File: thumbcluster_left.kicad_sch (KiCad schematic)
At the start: 12 parts, among them J1 Conn_01x06_Female, J2 Conn_01x06_Female, SW1 SW_Push, SW2 SW_Push, SW3 SW_Push, SW4 SW_Push, SW5 SW_Push

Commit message: Through hole switches
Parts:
- SW1, SW2, SW3, SW4, SW5: footprint keyswitches:Kailh_socket_MX -> keyswitches:SW_MX
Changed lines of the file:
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@@
     (property "Reference" "SW2" (id 0) (at 90.17 55.245 0))
     (property "Value" "SW_Push" (id 1) (at 90.17 57.785 0))
-    (property "Footprint" "keyswitches:Kailh_socket_MX" (id 2) (at 90.17 58.42 0)
+    (property "Footprint" "keyswitches:SW_MX" (id 2) (at 90.17 58.42 0)
       (effects (font (size 1.27 1.27)) hide)
     )
@@
     (property "Reference" "SW3" (id 0) (at 113.03 55.245 0))
     (property "Value" "SW_Push" (id 1) (at 113.03 57.785 0))
-    (property "Footprint" "keyswitches:Kailh_socket_MX" (id 2) (at 113.03 58.42 0)
+    (property "Footprint" "keyswitches:SW_MX" (id 2) (at 113.03 58.42 0)
       (effects (font (size 1.27 1.27)) hide)
     )
@@
     (property "Reference" "SW4" (id 0) (at 136.525 55.245 0))
     (property "Value" "SW_Push" (id 1) (at 136.525 57.785 0))
-    (property "Footprint" "keyswitches:Kailh_socket_MX" (id 2) (at 136.525 58.42 0)
+    (property "Footprint" "keyswitches:SW_MX" (id 2) (at 136.525 58.42 0)
       (effects (font (size 1.27 1.27)) hide)
     )
@@
     (property "Reference" "SW1" (id 0) (at 62.865 55.245 0))
     (property "Value" "SW_Push" (id 1) (at 62.865 57.785 0))
-    (property "Footprint" "keyswitches:Kailh_socket_MX" (id 2) (at 62.865 58.42 0)
+    (property "Footprint" "keyswitches:SW_MX" (id 2) (at 62.865 58.42 0)
       (effects (font (size 1.27 1.27)) hide)
     )
@@
     (property "Reference" "SW5" (id 0) (at 161.925 54.61 0))
     (property "Value" "SW_Push" (id 1) (at 161.925 57.15 0))
-    (property "Footprint" "keyswitches:Kailh_socket_MX" (id 2) (at 161.925 57.785 0)
+    (property "Footprint" "keyswitches:SW_MX" (id 2) (at 161.925 57.785 0)
       (effects (font (size 1.27 1.27)) hide)
     )
@@
     )
     (path "/85b19fe2-44d2-475f-bbc1-af68021ea01a"
-      (reference "SW1") (unit 1) (value "SW_Push") (footprint "keyswitches:Kailh_socket_MX")
+      (reference "SW1") (unit 1) (value "SW_Push") (footprint "keyswitches:SW_MX")
     )
     (path "/0c81e866-4681-43a4-aa9d-b943506b0b37"
-      (reference "SW2") (unit 1) (value "SW_Push") (footprint "keyswitches:Kailh_socket_MX")
+      (reference "SW2") (unit 1) (value "SW_Push") (footprint "keyswitches:SW_MX")
     )
     (path "/18a7139e-6ff8-49c2-a6d5-d2f8a6857830"
-      (reference "SW3") (unit 1) (value "SW_Push") (footprint "keyswitches:Kailh_socket_MX")
+      (reference "SW3") (unit 1) (value "SW_Push") (footprint "keyswitches:SW_MX")
     )
     (path "/8185e278-47e0-4401-93fe-75e7b14ab53c"
-      (reference "SW4") (unit 1) (value "SW_Push") (footprint "keyswitches:Kailh_socket_MX")
+      (reference "SW4") (unit 1) (value "SW_Push") (footprint "keyswitches:SW_MX")
     )
     (path "/ecba316e-704e-4ac5-90f8-4ebc6db6ba65"
-      (reference "SW5") (unit 1) (value "SW_Push") (footprint "keyswitches:Kailh_socket_MX")
-    )
-  )
+      (reference "SW5") (unit 1) (value "SW_Push") (footprint "keyswitches:SW_MX")
+    )
+  )

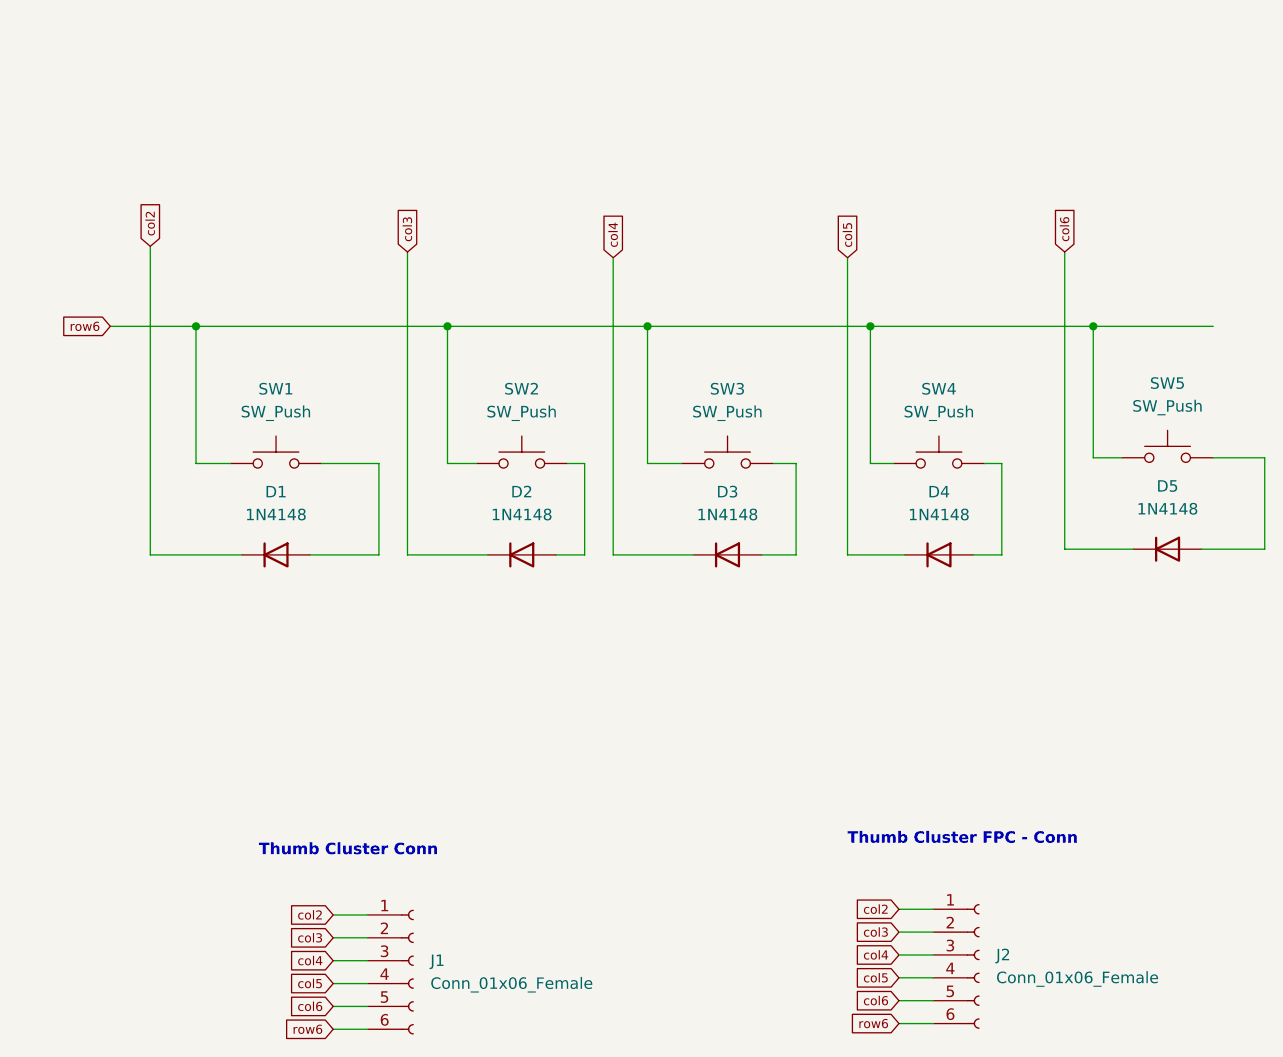
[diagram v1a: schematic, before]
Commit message: Complete net refactor
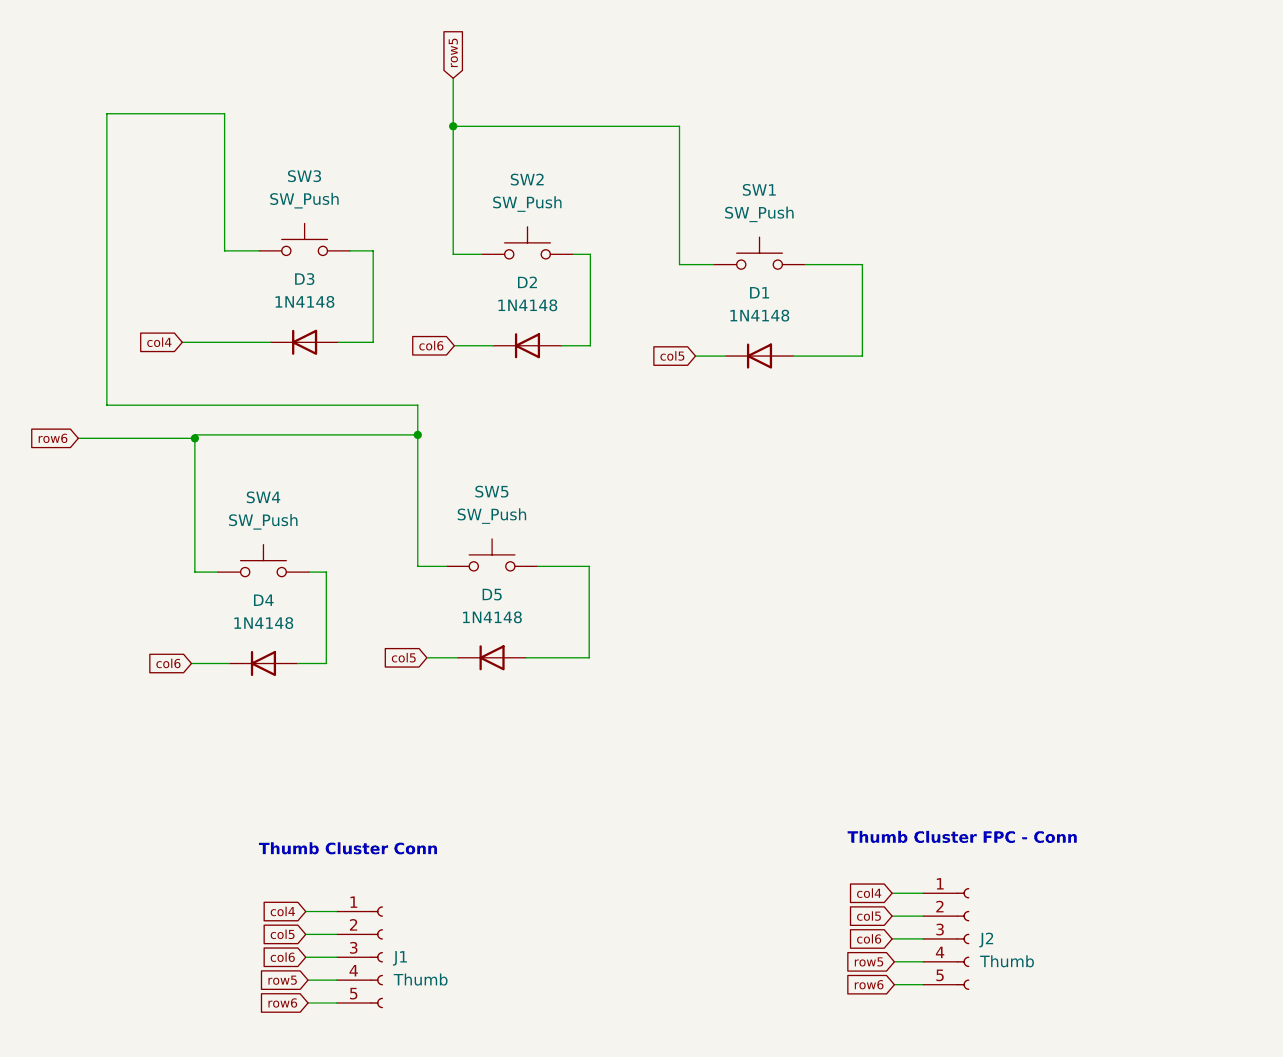
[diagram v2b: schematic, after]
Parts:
- removed J1: Conn_01x06_Female, Connector_PinSocket_2.00mm:PinSocket_1x06_P2.00mm_Vertical, symbol Connector:Conn_01x06_Female
- removed J2: Conn_01x06_Female, Connector_FFC-FPC:Molex_200528-0060_1x06-1MP_P1.00mm_Horizontal, symbol Connector:Conn_01x06_Female
- added J1: Thumb, Connector_PinSocket_2.00mm:PinSocket_1x05_P2.00mm_Vertical, symbol Connector:Conn_01x05_Female
- added J2: Thumb, Connector_FFC-FPC:Molex_200528-0050_1x05-1MP_P1.00mm_Horizontal, symbol Connector:Conn_01x05_Female
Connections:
- net col2 is gone; now on net col5: D1.1 (K)
- net col3 is gone; now on net col6: D2.1 (K)
- net col4: now also J1.1 (Pin_1), J2.1 (Pin_1)
- net col5: now also D5.1 (K), J1.2 (Pin_2), J2.2 (Pin_2); no longer D4.1 (K)
- net col6: now also D4.1 (K), J1.3 (Pin_3), J2.3 (Pin_3); no longer D5.1 (K)
- net row6: now also J1.5 (Pin_5), J2.5 (Pin_5); no longer SW1.1, SW2.1
- new net row5: J1.4 (Pin_4), J2.4 (Pin_4), SW1.1, SW2.1
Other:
- moved on the sheet: D1, D2, D3, D4, D5, SW1, SW2, SW3, SW4, SW5
